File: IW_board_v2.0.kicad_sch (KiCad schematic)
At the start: 0 parts

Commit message: Rev 1.0
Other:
- title: (none) -> Iron Warriors v2.0 

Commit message: Initial PCB view
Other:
- sheet CPU ports: added GPIO20, GPIO21, GPIO22, GPIO23, GPIO24, GPIO25; removed none
- sheet IO ports: added EMU, GPIO20, GPIO21, GPIO22, GPIO23, GPIO24, GPIO25, IGN, INJ, STARTER; removed none
- sheet PWR ports: added EMU, IGN, INJ, STARTER; removed none

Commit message: Small corrections
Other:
- sheet CPU ports: added GPIO10; removed GPIO23
- sheet IO ports: added 16V, GPIO10; removed GPIO23
- sheet PWR ports: added 16V; removed none

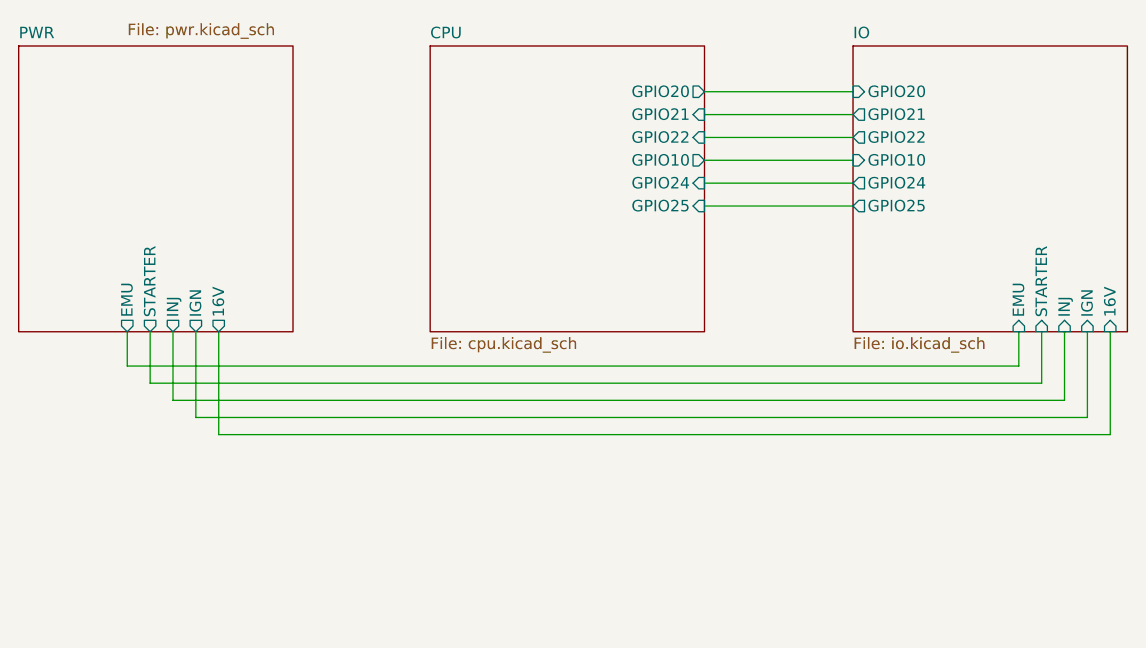
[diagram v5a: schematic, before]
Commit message: Added CAN transsiver to RP2040
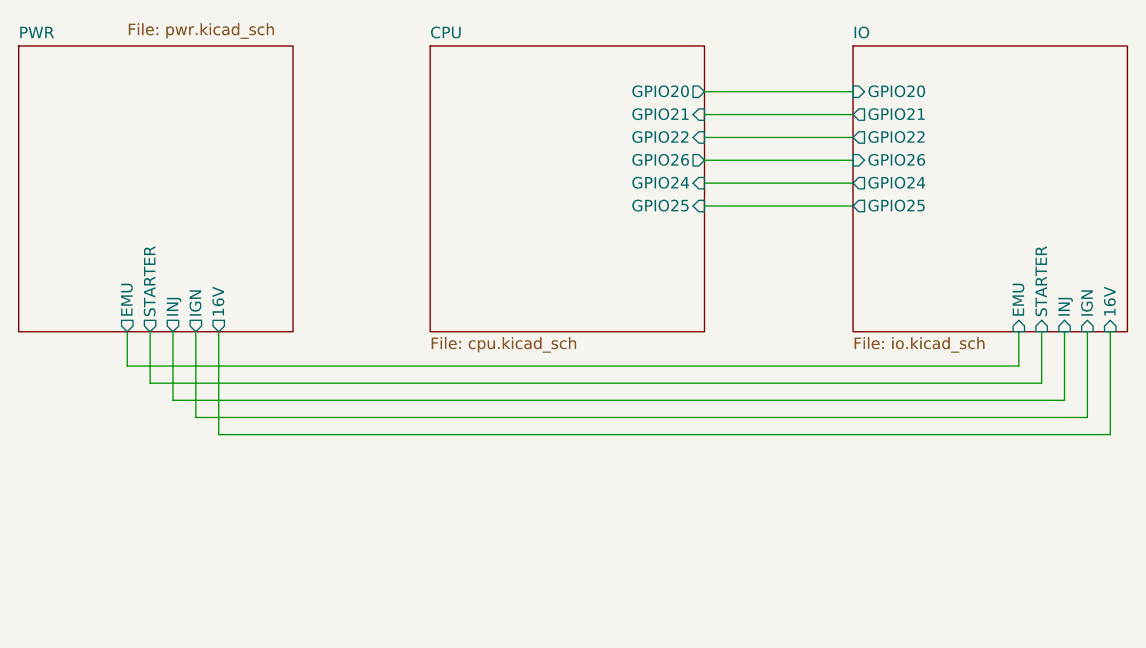
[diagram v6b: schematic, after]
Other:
- sheet CPU ports: added GPIO26; removed GPIO10
- sheet IO ports: added GPIO26; removed GPIO10
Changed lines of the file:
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@@
       (effects (font (size 1.27 1.27)) (justify left top))
     )
-    (pin "GPIO10" output (at 133.35 53.34 0)
+    (pin "GPIO26" output (at 133.35 53.34 0)
       (effects (font (size 1.27 1.27)) (justify right))
     )
@@
       (effects (font (size 1.27 1.27)) (justify left top))
     )
-    (pin "GPIO10" input (at 149.86 53.34 180)
+    (pin "GPIO26" input (at 149.86 53.34 180)
       (effects (font (size 1.27 1.27)) (justify left))
     )
@@
     (path "/b7b52878-fe66-484d-b159-40551c46f7bc" (page "3"))
     (path "/f17d7605-1e7d-42eb-aa0e-da1f84e26a35" (page "4"))
+    (path "/b7b52878-fe66-484d-b159-40551c46f7bc/3d3401f4-9fc2-4eb9-901a-9453ad25fb69" (page "5"))
   )
   (symbol_instances
@@
       (reference "#PWR036") (unit 1) (value "GND") (footprint "")
     )
-    (path "/f17d7605-1e7d-42eb-aa0e-da1f84e26a35/e7ef8b34-f2b4-4fcb-9351-341c96e6c1a7"
-      (reference "#PWR037") (unit 1) (value "+5V") (footprint "")
-    )
     (path "/f17d7605-1e7d-42eb-aa0e-da1f84e26a35/e4d17dc1-95fd-427f-9e16-b0dc8d668124"
       (reference "#PWR039") (unit 1) (value "GND") (footprint "")
@@
       (reference "#PWR0149") (unit 1) (value "GNDS") (footprint "")
     )
-    (path "/f17d7605-1e7d-42eb-aa0e-da1f84e26a35/aa148e21-3114-47dc-93ae-7f3edc526747"
-      (reference "#PWR0150") (unit 1) (value "GND") (footprint "")
-    )
     (path "/f17d7605-1e7d-42eb-aa0e-da1f84e26a35/1308515f-a03e-4490-afbc-132e2058455a"
       (reference "#PWR0151") (unit 1) (value "GND") (footprint "")
@@
       (reference "#PWR0152") (unit 1) (value "GND") (footprint "")
     )
+    (path "/f17d7605-1e7d-42eb-aa0e-da1f84e26a35/6b33a7c8-940b-4e17-91f8-f80cf3772521"
+      (reference "#PWR0153") (unit 1) (value "+5V") (footprint "")
+    )
+    (path "/f17d7605-1e7d-42eb-aa0e-da1f84e26a35/cec584a6-06da-4f84-96bf-6ddecddf7fd2"
+      (reference "#PWR0154") (unit 1) (value "GND") (footprint "")
+    )
+    (path "/b7b52878-fe66-484d-b159-40551c46f7bc/3d3401f4-9fc2-4eb9-901a-9453ad25fb69/1db8fd0f-1cab-4be2-97ea-5f4b39660da6"
+      (reference "#PWR0155") (unit 1) (value "+3.3V") (footprint "")
+    )
+    (path "/b7b52878-fe66-484d-b159-40551c46f7bc/3d3401f4-9fc2-4eb9-901a-9453ad25fb69/91f00e82-84e3-4f1d-934c-ff77e1464ae0"
+      (reference "#PWR0156") (unit 1) (value "+3.3V") (footprint "")
+    )
+    (path "/b7b52878-fe66-484d-b159-40551c46f7bc/3d3401f4-9fc2-4eb9-901a-9453ad25fb69/015e2b77-0c41-4128-99ec-e5d32584a6b0"
+      (reference "#PWR0157") (unit 1) (value "+3.3V") (footprint "")
+    )
+    (path "/b7b52878-fe66-484d-b159-40551c46f7bc/3d3401f4-9fc2-4eb9-901a-9453ad25fb69/4599d1d5-f17d-4e5e-ad96-60602466e310"
+      (reference "#PWR0158") (unit 1) (value "GND") (footprint "")
+    )
+    (path "/b7b52878-fe66-484d-b159-40551c46f7bc/3d3401f4-9fc2-4eb9-901a-9453ad25fb69/d885d9e4-c27c-43ec-b37e-63be6f5d9e78"
+      (reference "#PWR0159") (unit 1) (value "GND") (footprint "")
+    )
+    (path "/b7b52878-fe66-484d-b159-40551c46f7bc/3d3401f4-9fc2-4eb9-901a-9453ad25fb69/5b249fab-476b-4688-a1e1-d944ed8cb6e9"
+      (reference "#PWR0162") (unit 1) (value "+3.3V") (footprint "")
+    )
+    (path "/b7b52878-fe66-484d-b159-40551c46f7bc/3d3401f4-9fc2-4eb9-901a-9453ad25fb69/17d65cfe-1490-4729-b67f-2d855c18c2df"
+      (reference "#PWR0163") (unit 1) (value "GND") (footprint "")
+    )
+    (path "/b7b52878-fe66-484d-b159-40551c46f7bc/3d3401f4-9fc2-4eb9-901a-9453ad25fb69/8cdde7c5-8415-486d-bc6a-5abac91d045f"
+      (reference "#PWR0164") (unit 1) (value "+3.3V") (footprint "")
+    )
+    (path "/b7b52878-fe66-484d-b159-40551c46f7bc/3d3401f4-9fc2-4eb9-901a-9453ad25fb69/02e34764-11a6-42c3-9ba6-989825791407"
+      (reference "#PWR0165") (unit 1) (value "GND") (footprint "")
+    )
+    (path "/b7b52878-fe66-484d-b159-40551c46f7bc/3d3401f4-9fc2-4eb9-901a-9453ad25fb69/fc857fc0-82e2-4b1d-b5a2-931f374d16db"
+      (reference "#PWR0166") (unit 1) (value "GND") (footprint "")
+    )
+    (path "/b7b52878-fe66-484d-b159-40551c46f7bc/3d3401f4-9fc2-4eb9-901a-9453ad25fb69/f63b3084-3e3a-4d14-a4f1-eda610df7905"
+      (reference "#PWR0167") (unit 1) (value "GND") (footprint "")
+    )
     (path "/1d9d9a52-6d90-4bd5-bf76-ff1a6677f813/a09f6f75-d227-41fc-9c89-17fad6c8b61c"
       (reference "C1") (unit 1) (value "47uF") (footprint "Capacitor_SMD:CP_Elec_6.3x5.8")
@@
       (reference "C24") (unit 1) (value "0.1uF") (footprint "Capacitor_SMD:C_0603_1608Metric")
     )
+    (path "/b7b52878-fe66-484d-b159-40551c46f7bc/3d3401f4-9fc2-4eb9-901a-9453ad25fb69/0b7da5f3-d5bd-442c-97a6-4b8ef47fd839"
+      (reference "C25") (unit 1) (value "100nF") (footprint "Capacitor_SMD:C_0603_1608Metric")
+    )
+    (path "/b7b52878-fe66-484d-b159-40551c46f7bc/3d3401f4-9fc2-4eb9-901a-9453ad25fb69/bb241464-b7b4-4bde-aa5a-f36b81fdaad4"
+      (reference "C26") (unit 1) (value "10pF") (footprint "Capacitor_SMD:C_0603_1608Metric")
+    )
+    (path "/b7b52878-fe66-484d-b159-40551c46f7bc/3d3401f4-9fc2-4eb9-901a-9453ad25fb69/ea1e9e6e-9643-4536-afd5-277821207b62"
+      (reference "C27") (unit 1) (value "10pF") (footprint "Capacitor_SMD:C_0603_1608Metric")
+    )
+    (path "/b7b52878-fe66-484d-b159-40551c46f7bc/3d3401f4-9fc2-4eb9-901a-9453ad25fb69/3946a042-8062-440c-bab0-1d9a86cf3620"
+      (reference "C28") (unit 1) (value "100nF") (footprint "Capacitor_SMD:C_0603_1608Metric")
+    )
     (path "/1d9d9a52-6d90-4bd5-bf76-ff1a6677f813/36165b4c-a43a-4135-a080-c5a00cec3bb1"
       (reference "D1") (unit 1) (value "B120-E3") (footprint "Diode_SMD:D_SMA")
@@
     )
     (path "/1d9d9a52-6d90-4bd5-bf76-ff1a6677f813/69443c54-d367-4f66-af31-dc803530e951"
-      (reference "F9") (unit 1) (value "7.5V 5A") (footprint "FUSE_3557-2:FUSE_3557-2")
+      (reference "F9") (unit 1) (value "16V 5A") (footprint "FUSE_3557-2:FUSE_3557-2")
     )
     (path "/b7b52878-fe66-484d-b159-40551c46f7bc/617d77ee-89ad-468f-a3f9-f0b79fff4d62"
@@
       (reference "J27") (unit 1) (value "CLT CON") (footprint "TerminalBlock_Phoenix:TerminalBlock_Phoenix_MPT-0,5-2-2.54_1x02_P2.54mm_Horizontal")
     )
+    (path "/f17d7605-1e7d-42eb-aa0e-da1f84e26a35/01de0786-a926-4b7e-b92a-7c05da65a01b"
+      (reference "J28") (unit 1) (value "TPS CON") (footprint "TerminalBlock_Phoenix:TerminalBlock_Phoenix_MPT-0,5-3-2.54_1x03_P2.54mm_Horizontal")
+    )
     (path "/f17d7605-1e7d-42eb-aa0e-da1f84e26a35/2480914f-7e50-4376-8b6f-dd3fec58813f"
       (reference "K1") (unit 1) (value "FINDER-34.51 INJ") (footprint "Relay_THT:Relay_SPDT_Finder_34.51_Vertical")
@@
       (reference "R17") (unit 1) (value "330") (footprint "Resistor_SMD:R_0603_1608Metric")
     )
+    (path "/b7b52878-fe66-484d-b159-40551c46f7bc/3d3401f4-9fc2-4eb9-901a-9453ad25fb69/2495ab6d-dce7-462a-a42c-af6c1b107604"
+      (reference "R18") (unit 1) (value "10k") (footprint "Resistor_SMD:R_0603_1608Metric")
+    )
+    (path "/b7b52878-fe66-484d-b159-40551c46f7bc/3d3401f4-9fc2-4eb9-901a-9453ad25fb69/bda9489e-8a64-40cf-879b-d73362e30c2f"
+      (reference "R19") (unit 1) (value "10k") (footprint "Resistor_SMD:R_0603_1608Metric")
+    )
+    (path "/b7b52878-fe66-484d-b159-40551c46f7bc/3d3401f4-9fc2-4eb9-901a-9453ad25fb69/ab7264fb-d072-4028-a8bb-787c4777360e"
+      (reference "R20") (unit 1) (value "10k") (footprint "Resistor_SMD:R_0603_1608Metric")
+    )
     (path "/b7b52878-fe66-484d-b159-40551c46f7bc/e4bf569e-61a1-4f73-bdfd-6440192b0692"
       (reference "SW1") (unit 1) (value "TL3342F160QG/TR") (footprint "TL3342F160QG_TR:SW_TL3342F160QG%2fTR")
@@
       (reference "U7") (unit 1) (value "TXS0108EPWR") (footprint "TXS0108EPWR:SOP65P640X120-20N")
     )
-    (path "/f17d7605-1e7d-42eb-aa0e-da1f84e26a35/5bf3ab7c-9c44-4f6b-8e06-2a4d9eb60503"
-      (reference "U8") (unit 1) (value "2EDN7524F") (footprint "2EDN7524F:SOIC127P600X175-8N-22-V")
+    (path "/b7b52878-fe66-484d-b159-40551c46f7bc/3d3401f4-9fc2-4eb9-901a-9453ad25fb69/8ada2a5a-7658-4825-be96-66febb90e57a"
+      (reference "U9") (unit 1) (value "MCP2515") (footprint "Package_SO:SOIC-18W_7.5x11.6mm_P1.27mm")
+    )
+    (path "/b7b52878-fe66-484d-b159-40551c46f7bc/3d3401f4-9fc2-4eb9-901a-9453ad25fb69/6ff3d66b-f1bf-449b-b586-fab672ef63e8"
+      (reference "U10") (unit 1) (value "SN65HVD232") (footprint "Package_SO:SOIC-8_3.9x4.9mm_P1.27mm")
     )
     (path "/b7b52878-fe66-484d-b159-40551c46f7bc/8c0fee58-aecf-495a-be5e-44bd965a69b1"
       (reference "Y1") (unit 1) (value "Crystal") (footprint "Crystal:Crystal_SMD_3225-4Pin_3.2x2.5mm")
     )
+    (path "/b7b52878-fe66-484d-b159-40551c46f7bc/3d3401f4-9fc2-4eb9-901a-9453ad25fb69/339b04a9-e063-44ca-91c5-02edf2f55b52"
+      (reference "Y2") (unit 1) (value "Crystal") (footprint "Crystal:Crystal_SMD_3225-4Pin_3.2x2.5mm")
+    )
   )
